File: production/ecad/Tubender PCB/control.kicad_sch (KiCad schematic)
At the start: 2 parts, among them U2 ESP32-WROOM-32UE_M113EH6400UH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, U7 MCP23017_GPIO_EXPANDER

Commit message: MCU and such
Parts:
- removed U7: MCP23017_GPIO_EXPANDER, symbol MCP23017:MCP23017_GPIO_EXPANDER
- added U3: MCP23017_GPIO_EXPANDER, symbol MCP23017:MCP23017_GPIO_EXPANDER
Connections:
- net 3V3: now also U3.9 (VDD)
- net EXPANDER_SCK: now also U3.12 (SCK)
- net EXPANDER_SDA: now also U3.13 (SDA/SI)
- net GND: now also U3.10 (VSS), U3.15 (A0), U3.16 (A1), U3.17 (A2)

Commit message: More MCU Stuff
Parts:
- added J1: USB4110GFA, USB4110GFA:GCT_USB4110GFA, symbol USB4110GFA:USB4110GFA
- added U4: MCP2221A-I_SL, MCP2221A-I_SL:SOIC127P600X175-14N, symbol MCP2221A-I_SL:MCP2221A-I_SL
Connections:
- net GND: now also J1.A1/B12 (GND), J1.B1/A12 (GND__1), J1.S1 (GND__2), J1.S2 (GND__3), J1.S3 (GND__4), J1.S4 (GND__5)
- net ESP_RX: now reaches U2.34 (RXD0)
- net ESP_RX: now also U4.5 (URX)
- net ESP_TX: now reaches U2.35 (TXD0)
- net ESP_TX: now also U4.6 (UTX)
- new net USB_+5V: J1.A4/B9 (VBUS), U4.1 (VDD)
- new net USB_D+: J1.A6 (DP1), U4.13 (D+)
- new net USB_D-: J1.A7 (DN1), U4.12 (D-)
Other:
- moved on the sheet: U2, U3

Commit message: MCU Rev1 Complete
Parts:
- removed U3: MCP23017_GPIO_EXPANDER, symbol MCP23017:MCP23017_GPIO_EXPANDER
- removed U4: MCP2221A-I_SL, MCP2221A-I_SL:SOIC127P600X175-14N, symbol MCP2221A-I_SL:MCP2221A-I_SL
- added C1, C2, C8: 0.1uF, symbol Device:C
- added C3, C4: 10uF, symbol Device:C
- added C5: 10nF, symbol Device:C
- added C6, C7: 47pF, symbol Device:C
- added C9: 1nF, symbol Device:C
- added D1: 1N5819HW-7-F, 1N5819HW-7-F:SOD3715X145N, symbol 1N5819HW-7-F:1N5819HW-7-F
- added D2, D3: RCLAMP1521P.TCT, TVS_DFN2_SLP1006P2_SEM, symbol RCLAMP1521P:RCLAMP1521P.TCT
- added D4: GREEN, WL-SMCW_0603:WL-SMCW_0603, symbol WL-SMCW_0603:WL-SMCW_0603
- added D5: BLUE, WL-SMCW_0603:WL-SMCW_0603, symbol WL-SMCW_0603:WL-SMCW_0603
- added Q1, Q2: AO3400A, AO3400A:SOT95P280X125-3N, symbol AO3400A:AO3400A
- added R10, R8, R9: 10K, symbol Device:R_US
- added R11, R12, R13, R14, R15, R16: 0, symbol Device:R_US
- added R17, R18: 50, symbol Device:R_US
- added R19: 12K, symbol Device:R_US
- added R4, R5: 2K, symbol Device:R_US
- added R6, R7: 5.1K, symbol Device:R_US
- added S1: JS202011JCQN, JS202011JCQN:SW_JS202011JCQN, symbol JS202011JCQN:JS202011JCQN
- added S2, S3: TS02-66-70-BK, TS02-66-70-BK-260-LCR-D:SW_TS02-66-70-BK-260-LCR-D, symbol TS02-66-70-BK-260-LCR-D:TS02-66-70-BK-260-LCR-D
- added U3: MCP23017-E_SO, MCP23017-E_SO:SOIC127P1030X265-28N, symbol MCP23017-E_SO:MCP23017-E_SO
- added U4: FT232RL-REEL, FT232RL-REEL:SOP65P780X200-28N, symbol FT232RL-REEL:FT232RL-REEL
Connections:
- net USB_D+ is gone; now on an unnamed net: J1.A6 (DP1)
- net USB_D- is gone; now on an unnamed net: J1.A7 (DN1)
- net 3V3: now also C1.1, C2.1, C3.1, C4.1, R19.2, R4.2, R5.2, U3.9 (VDD)
- net EXPANDER_SCK: now also S1.5, U3.12 (SCK); no longer U2.36 (IO22)
- net EXPANDER_SDA: now also S1.1, U3.13 (SDA); no longer U2.33 (IO21)
- net GND: now also C1.2, C2.2, C3.2, C4.2, C5.2, C6.2, C7.2, C8.2, C9.2, D2.1, D3.1, R17.2, R18.2, R6.1, R7.1, U3.10 (VSS), U3.15 (A0), U3.16 (A1), U3.17 (A2), U4.18 (GND__1), U4.21 (GND__2), U4.25 (AGND), U4.26 (TEST), U4.7 (GND)
- net GPIO_0: now reaches U2.25 (IO0)
- net GPIO_0: now also R12.2, S2.1
- net ESP_EN: now reaches U2.3 (EN)
- net ESP_EN: now also C9.1, R11.2, R19.1, S3.1
- net BENDING_ENA: now reaches U2.30 (IO18)
- net at J1.A5 (CC1): now also R6.2
- net at J1.B5 (CC2): now also R7.2
- net at J1.B6 (DP2): now also C6.1, D3.2, U4.15 (USBDP)
- net at J1.B7 (DN2): now also C7.1, D2.2, U4.16 (USBDM)
- net ESP_RX renamed ESP_RXD0
- net ESP_RXD0: now also R13.1
- net ESP_TX renamed ESP_TXD0
- net ESP_TXD0: now also R14.1
- net USB_+5V: no longer names the net of J1.A4/B9 (VBUS)
- net USB_+5V: now also D1.A
- new net: Q1.1, Q2.2, R9.2
- new net: Q1.2, Q2.1, R10.2
- new net: Q1.3, R11.1
- new net: R18.1, S3.4
- new net: Q2.3, R12.1
- new net: R8.1, U4.19 (~{RESET})
- new net: C5.1, D1.C, U4.20 (VCC)
- new net: D4.2, R4.1
- new net: R17.1, S2.4
- new net: D4.1, U4.23 (CBUS0)
- new net: C8.1, U4.17 (3V3OUT), U4.4 (VCCIO)
- new net: D5.1, U4.22 (CBUS1)
- new net: D5.2, R5.1
- new net 5V: R8.2
- new net ADVANCE_LIMIT_1: U3.23 (GPA2)
- new net ADVANCE_LIMIT_2: U3.24 (GPA3)
- new net BOOT_SCK: R10.1, S1.7, U4.3 (~{RTS})
- new net BOOT_SDA: S1.3, U4.11 (~{CTS})
- new net CHUCK_BEAM: U3.26 (GPA5)
- new net DIE_BEAM: U3.25 (GPA4)
- new net DIE_LIMIT_1: U3.21 (GPA0)
- new net DIE_LIMIT_2: U3.22 (GPA1)
- new net DTR: R9.1, U4.2 (~{DTR})
- new net ESP_RXD: R13.2, U4.1 (TXD)
- new net ESP_SCK: R16.2, S1.6
- new net ESP_SCK_OUT: R16.1, U2.36 (IO22)
- new net ESP_SDA: R15.2, S1.2
- new net ESP_SDA_OUT: R15.1, U2.33 (IO21)
- new net ESP_TXD: R14.2, U4.5 (RXD)
- no-connect marks 0 -> 14
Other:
- note added: "ESP32"
- note added: "Flash/Boot Functionality"
- note added: "GPIO Expansion"
- note added: "USB to UART"
- moved on the sheet: J1, U2

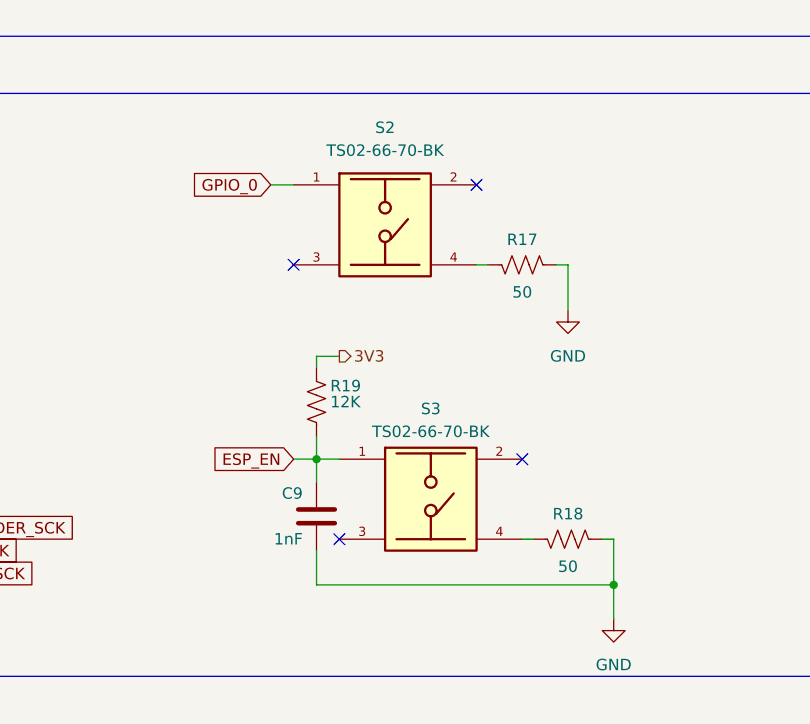
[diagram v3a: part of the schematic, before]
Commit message: Fixed a Switch or 2
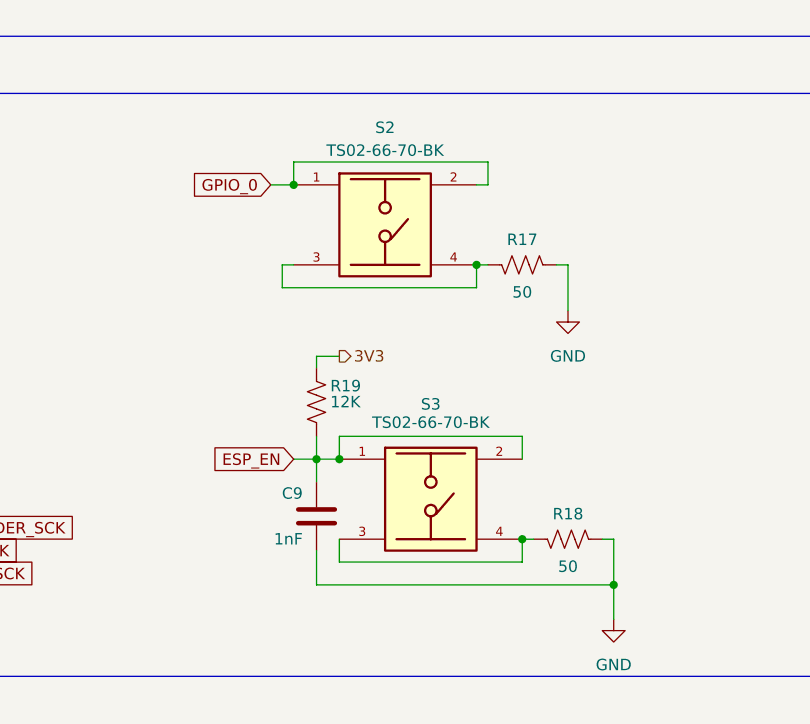
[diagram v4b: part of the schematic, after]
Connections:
- net ESP_EN: now also S3.2
- net GPIO_0: now also S2.2
- net at S3.3: now also R18.1, S3.4
- net at S2.3: now also R17.1, S2.4
- no-connect marks 14 -> 10
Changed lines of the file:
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@@
 	)
 	(junction
+		(at 222.25 109.22)
+		(diameter 0)
+		(color 0 0 0 0)
+	)
+	(junction
 		(at 97.79 105.41)
 		(diameter 0)
@@
 	)
 	(junction
+		(at 247.65 148.59)
+		(diameter 0)
+		(color 0 0 0 0)
+	)
+	(junction
 		(at 160.02 114.3)
 		(diameter 0)
@@
 	)
 	(junction
+		(at 227.33 139.7)
+		(diameter 0)
+		(color 0 0 0 0)
+	)
+	(junction
 		(at 217.17 73.66)
 		(diameter 0)
 		(color 0 0 0 0)
 	)
-	(no_connect
-		(at 152.4 57.15)
+	(junction
+		(at 242.57 118.11)
+		(diameter 0)
+		(color 0 0 0 0)
 	)
 	(no_connect
-		(at 247.65 139.7)
+		(at 152.4 57.15)
 	)
 	(no_connect
@@
 	)
 	(no_connect
-		(at 222.25 118.11)
-	)
-	(no_connect
 		(at 152.4 59.69)
 	)
@@
 	)
 	(no_connect
-		(at 227.33 148.59)
-	)
-	(no_connect
 		(at 152.4 44.45)
 	)
@@
 	)
 	(no_connect
-		(at 242.57 109.22)
-	)
-	(no_connect
 		(at 152.4 52.07)
 	)
@@
 	(wire
 		(pts
+			(xy 227.33 151.13) (xy 247.65 151.13)
+		)
+		(stroke
+			(width 0)
+			(type default)
+		)
+	)
+	(wire
+		(pts
 			(xy 157.48 68.58) (xy 157.48 64.77)
 		)
@@
 		)
 	)
+	(wire
+		(pts
+			(xy 243.84 106.68) (xy 243.84 109.22)
+		)
+		(stroke
+			(width 0)
+			(type default)
+		)
+	)
 	(polyline
 		(pts
@@
 	(wire
 		(pts
+			(xy 247.65 148.59) (xy 247.65 151.13)
+		)
+		(stroke
+			(width 0)
+			(type default)
+		)
+	)
+	(wire
+		(pts
 			(xy 156.21 124.46) (xy 158.75 124.46)
 		)
@@
 	(wire
 		(pts
+			(xy 227.33 137.16) (xy 247.65 137.16)
+		)
+		(stroke
+			(width 0)
+			(type default)
+		)
+	)
+	(wire
+		(pts
 			(xy 119.38 39.37) (xy 119.38 62.23)
 		)
@@
 	(wire
 		(pts
+			(xy 220.98 120.65) (xy 242.57 120.65)
+		)
+		(stroke
+			(width 0)
+			(type default)
+		)
+	)
+	(wire
+		(pts
 			(xy 83.82 67.31) (xy 95.25 67.31)
 		)
@@
 	(wire
 		(pts
+			(xy 222.25 106.68) (xy 243.84 106.68)
+		)
+		(stroke
+			(width 0)
+			(type default)
+		)
+	)
+	(wire
+		(pts
 			(xy 260.35 33.02) (xy 254 33.02)
 		)
@@
 	(wire
 		(pts
+			(xy 247.65 139.7) (xy 247.65 137.16)
+		)
+		(stroke
+			(width 0)
+			(type default)
+		)
+	)
+	(wire
+		(pts
 			(xy 30.48 52.07) (xy 30.48 54.61)
 		)
@@
 	(wire
 		(pts
+			(xy 242.57 120.65) (xy 242.57 118.11)
+		)
+		(stroke
+			(width 0)
+			(type default)
+		)
+	)
+	(wire
+		(pts
 			(xy 256.54 53.34) (xy 254 53.34)
 		)
@@
 	(wire
 		(pts
+			(xy 227.33 137.16) (xy 227.33 139.7)
+		)
+		(stroke
+			(width 0)
+			(type default)
+		)
+	)
+	(wire
+		(pts
+			(xy 222.25 118.11) (xy 220.98 118.11)
+		)
+		(stroke
+			(width 0)
+			(type default)
+		)
+	)
+	(wire
+		(pts
 			(xy 251.46 118.11) (xy 252.73 118.11)
 		)
@@
 	(wire
 		(pts
+			(xy 220.98 118.11) (xy 220.98 120.65)
+		)
+		(stroke
+			(width 0)
+			(type default)
+		)
+	)
+	(wire
+		(pts
 			(xy 121.92 64.77) (xy 87.63 64.77)
 		)
@@
 	(wire
 		(pts
+			(xy 227.33 148.59) (xy 227.33 151.13)
+		)
+		(stroke
+			(width 0)
+			(type default)
+		)
+	)
+	(wire
+		(pts
 			(xy 243.84 118.11) (xy 242.57 118.11)
 		)
@@
 	(wire
 		(pts
+			(xy 222.25 109.22) (xy 222.25 106.68)
+		)
+		(stroke
+			(width 0)
+			(type default)
+		)
+	)
+	(wire
+		(pts
 			(xy 224.79 149.86) (xy 224.79 153.67)
 		)
@@
 	(wire
 		(pts
+			(xy 242.57 109.22) (xy 243.84 109.22)
+		)
+		(stroke
+			(width 0)
+			(type default)
+		)
+	)
+	(wire
+		(pts
 			(xy 179.07 73.66) (xy 177.8 73.66)
 		)
@@
 		(dnp no)
 		(property "Reference" "S3"
-			(at 237.49 134.112 0)
+			(at 237.49 133.604 0)
 			(effects
 				(font
@@
 		)
 		(property "Value" "TS02-66-70-BK"
-			(at 237.49 136.652 0)
+			(at 237.49 135.636 0)
 			(effects
 				(font

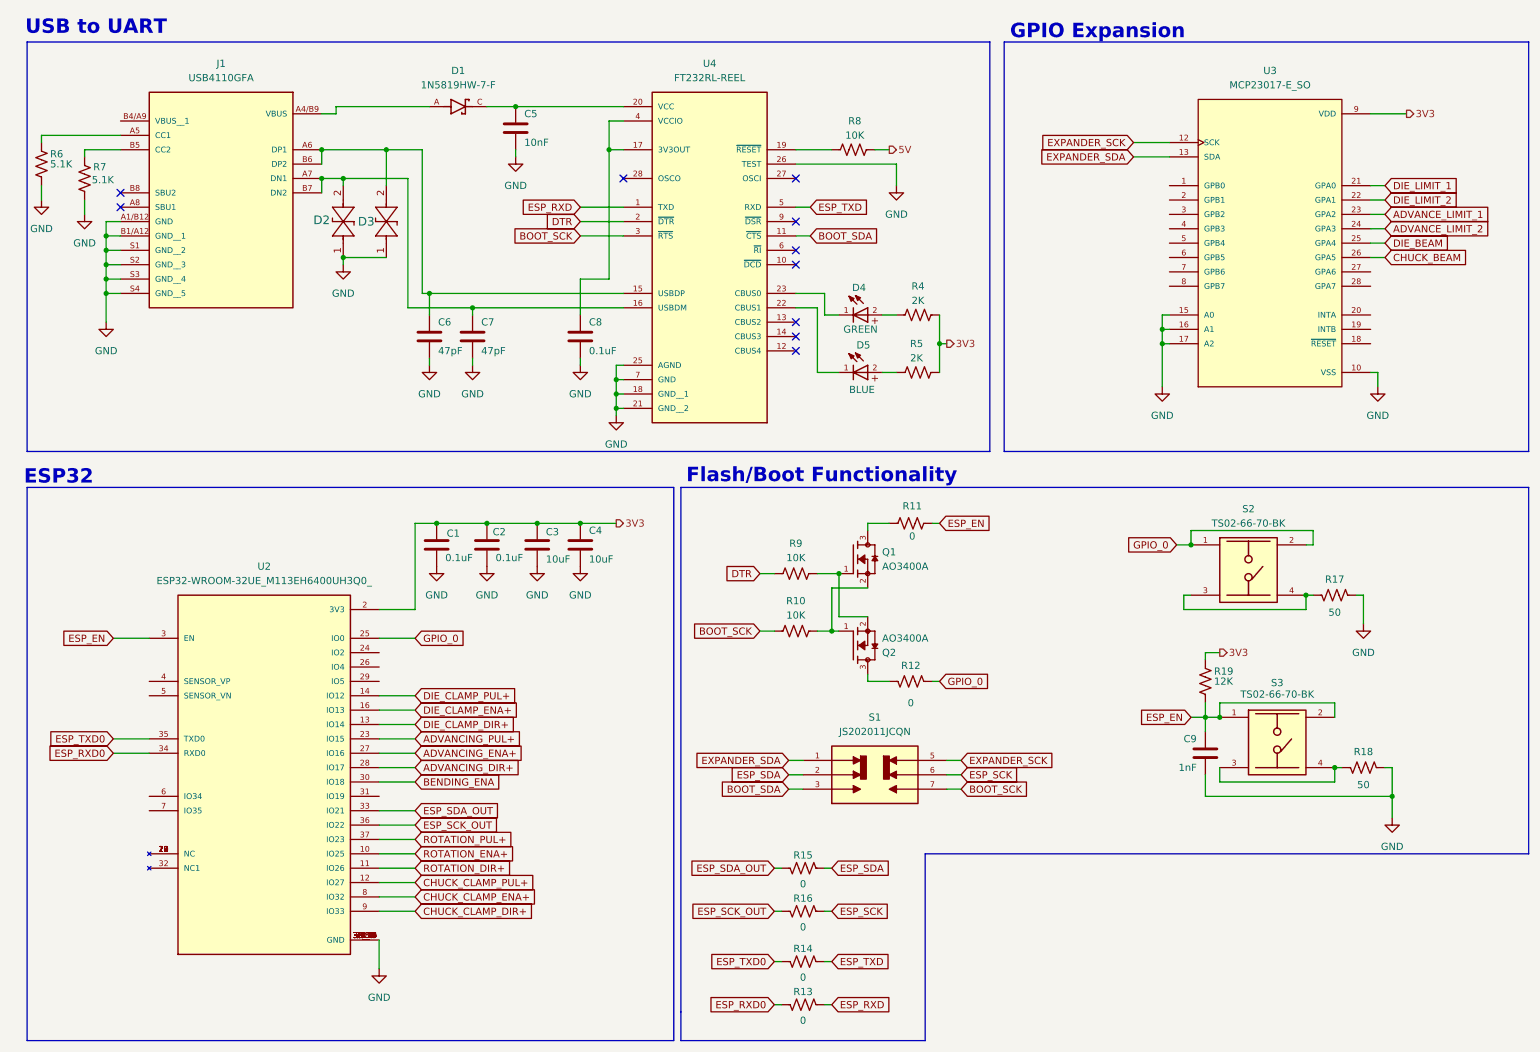
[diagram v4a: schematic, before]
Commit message: 7 Segment, Buttons, Plexers Oh MY!
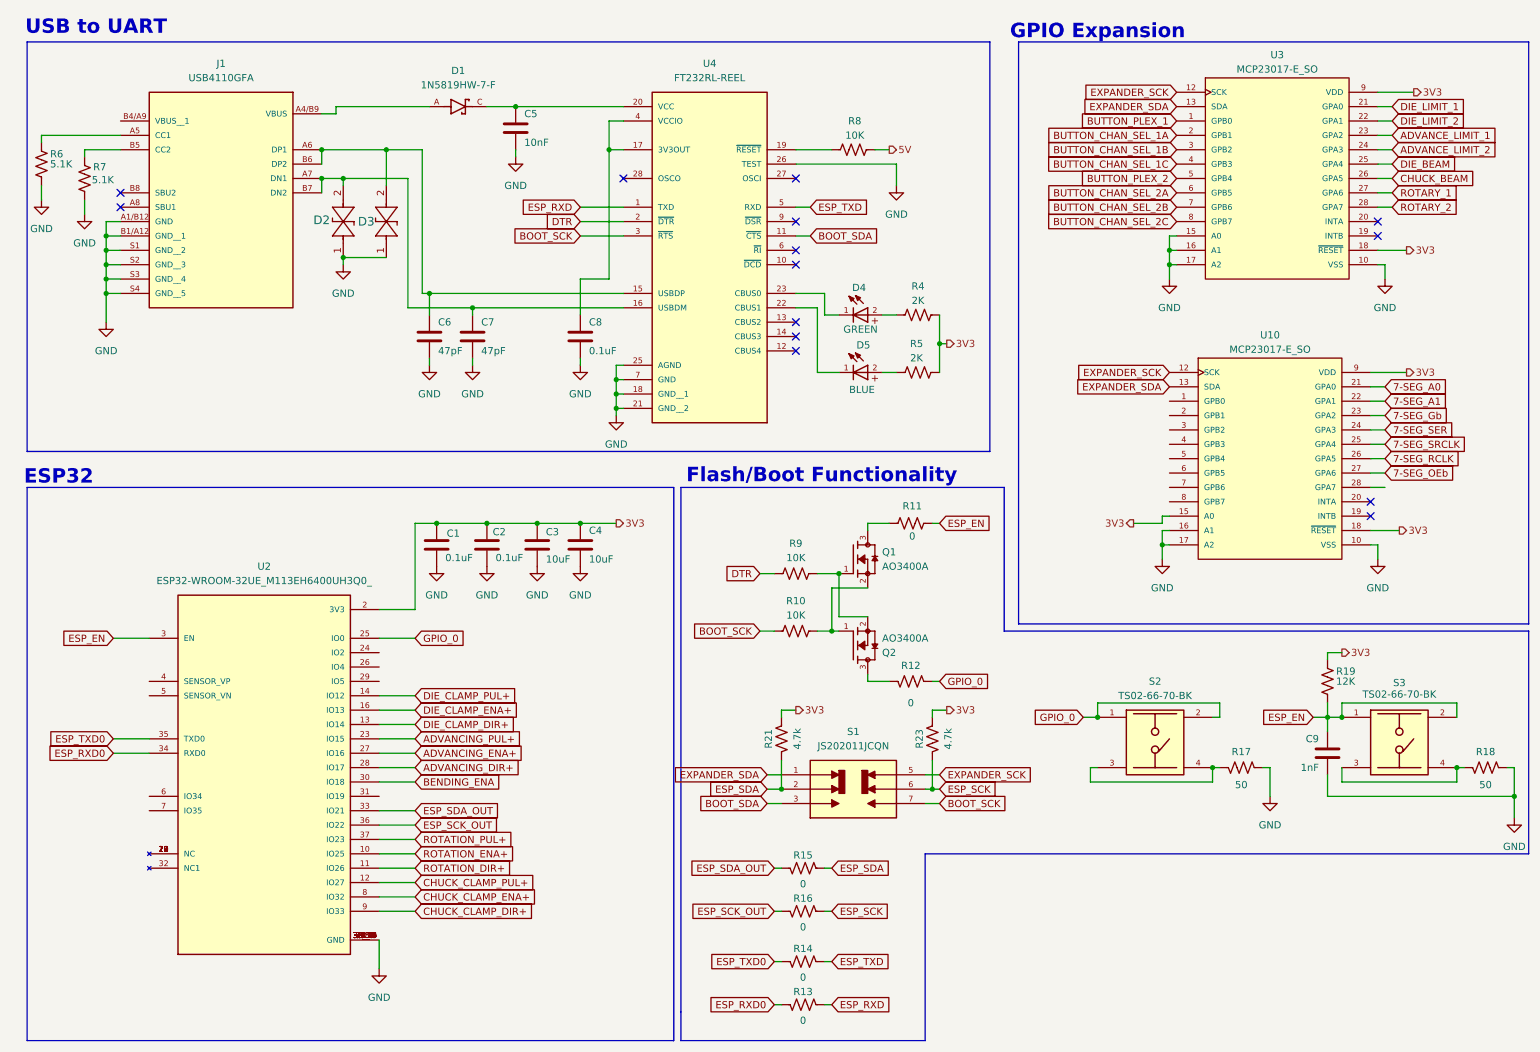
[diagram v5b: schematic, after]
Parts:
- added R21, R23: 4.7k, symbol Device:R_US
- added U10: MCP23017-E_SO, MCP23017-E_SO:SOIC127P1030X265-28N, symbol MCP23017-E_SO:MCP23017-E_SO
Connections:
- net 3V3: now also U3.18 (~{RESET}), R21.2, R23.2, U10.15 (A0), U10.18 (~{RESET}), U10.9 (VDD)
- net ESP_SCK: now also R23.1
- net ESP_SDA: now also R21.1
- net EXPANDER_SCK: now also U10.12 (SCK)
- net EXPANDER_SDA: now also U10.13 (SDA)
- net GND: now also U10.10 (VSS), U10.16 (A1), U10.17 (A2)
- net BUTTON_PLEX_1: now reaches U3.1 (GPB0)
- net BUTTON_CHAN_SEL_1A: now reaches U3.2 (GPB1)
- net ROTARY_1: now reaches U3.27 (GPA6)
- net ROTARY_2: now reaches U3.28 (GPA7)
- net BUTTON_CHAN_SEL_1B: now reaches U3.3 (GPB2)
- net BUTTON_CHAN_SEL_1C: now reaches U3.4 (GPB3)
- net BUTTON_PLEX_2: now reaches U3.5 (GPB4)
- net BUTTON_CHAN_SEL_2A: now reaches U3.6 (GPB5)
- net BUTTON_CHAN_SEL_2B: now reaches U3.7 (GPB6)
- net BUTTON_CHAN_SEL_2C: now reaches U3.8 (GPB7)
- new net 7-SEG_A0: U10.21 (GPA0)
- new net 7-SEG_A1: U10.22 (GPA1)
- new net 7-SEG_Gb: U10.23 (GPA2)
- new net 7-SEG_OEb: U10.27 (GPA6)
- new net 7-SEG_RCLK: U10.26 (GPA5)
- new net 7-SEG_SER: U10.24 (GPA3)
- new net 7-SEG_SRCLK: U10.25 (GPA4)
- no-connect marks 10 -> 14
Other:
- moved on the sheet: C9, R17, R18, R19, S1, S2, S3, U3
